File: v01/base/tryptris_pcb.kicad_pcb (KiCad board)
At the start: 2 copper layers, 298.8 x 122 mm, 142 parts, among them J1 USB_C_Receptacle_USB2.0, J2 I2C-L, J3 I2C-R, J4 AVR-ISP-6, SW1 Reset, U1 ATmega32U4-AU, U2 MCP23017_SO, U4 HOLE, Y1 16Mhz

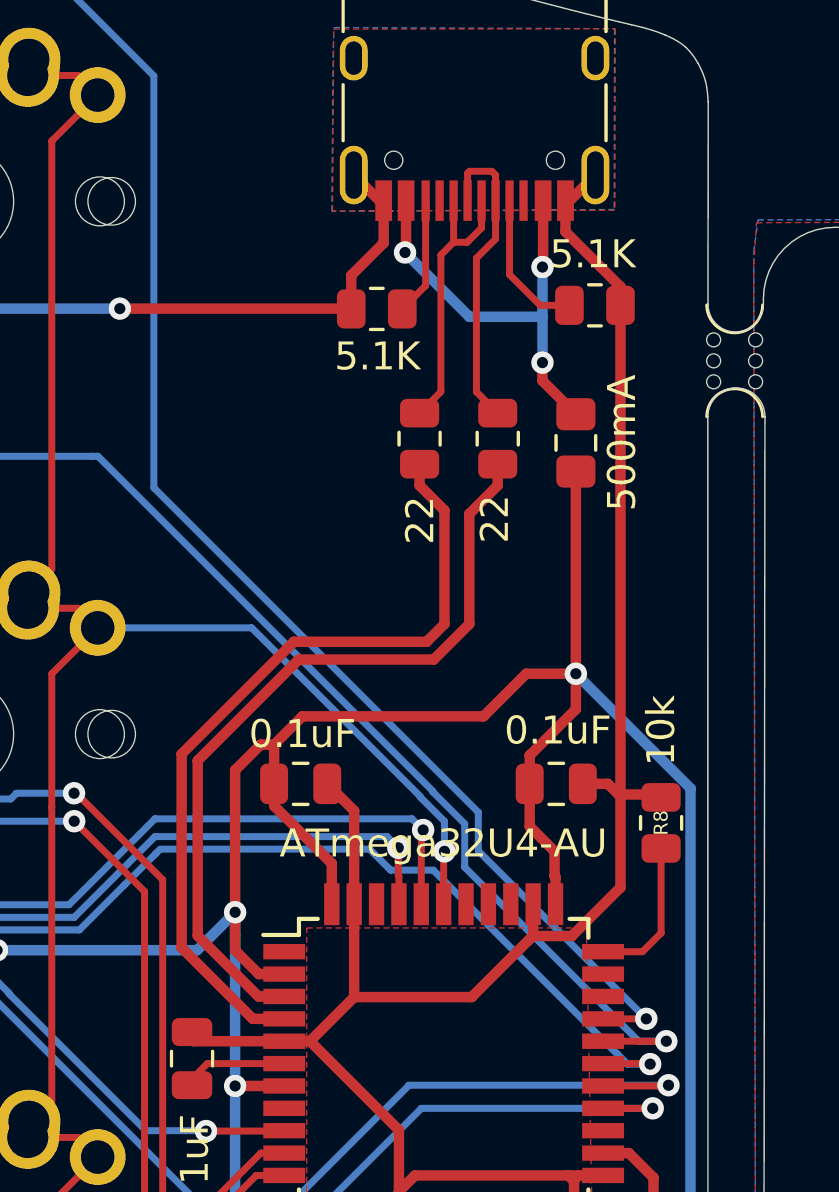
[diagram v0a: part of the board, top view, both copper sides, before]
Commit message: Add ESD component to both boards.
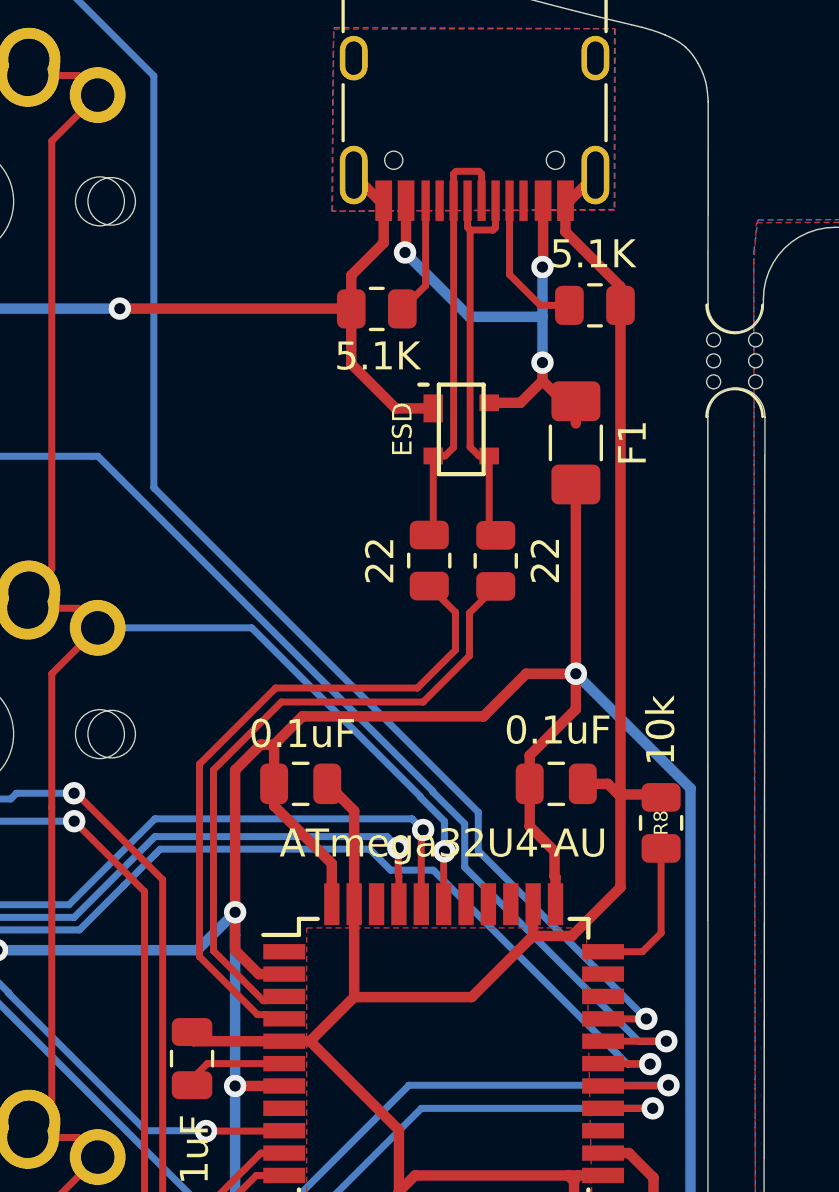
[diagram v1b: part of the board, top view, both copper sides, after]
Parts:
- added U3: PRTR5V0U2X, Keebio-Parts:SOT-143B, F.Cu at (149.2, 53.2)
- F1: footprint Fuse:Fuse_0805_2012Metric_Pad1.15x1.40mm_HandSolder -> Fuse:Fuse_1206_3216Metric_Pad1.42x1.75mm_HandSolder
- moved R5 4.37 mm to (148.0, 57.9), turned to 90 degrees
- moved R4 4.37 mm to (150.4, 57.9)
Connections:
- net Net-(J1-PadA7) renamed DN
- J1 pad A6: Net-(J1-PadA6) -> DP
- J1 pad B6: Net-(J1-PadA6) -> DP
- R5 pad 1: Net-(J1-PadA6) -> D+
- R5 pad 2: D+ -> DP
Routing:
- net DP: track 0.00 -> 15.6 mm
- net Net-(J1-PadA6): track 10.3 -> 0.00 mm
- net GND: track 188.7 -> 194.2 mm
- net D-: track 28.3 -> 23.5 mm
- net D+: track 29.1 -> 24.4 mm
- net DN: track 11.2 -> 14.5 mm
- net VCC: track 16.3 -> 18.6 mm
